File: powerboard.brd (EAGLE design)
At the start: 90 x 21 mm, 25 parts, among them IC1 ISL9122AIRNZ-T, U1 MCP73831T-2DCI/MC, U2 MIC826RYMT-TR

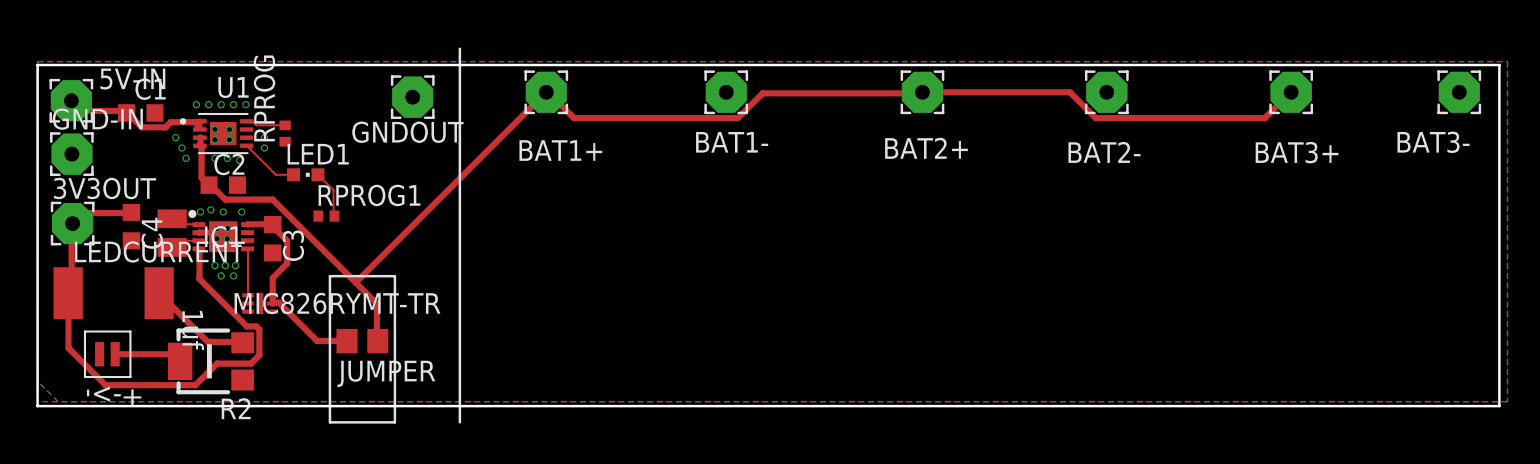
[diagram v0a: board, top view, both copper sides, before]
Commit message: update powerboard with fixes
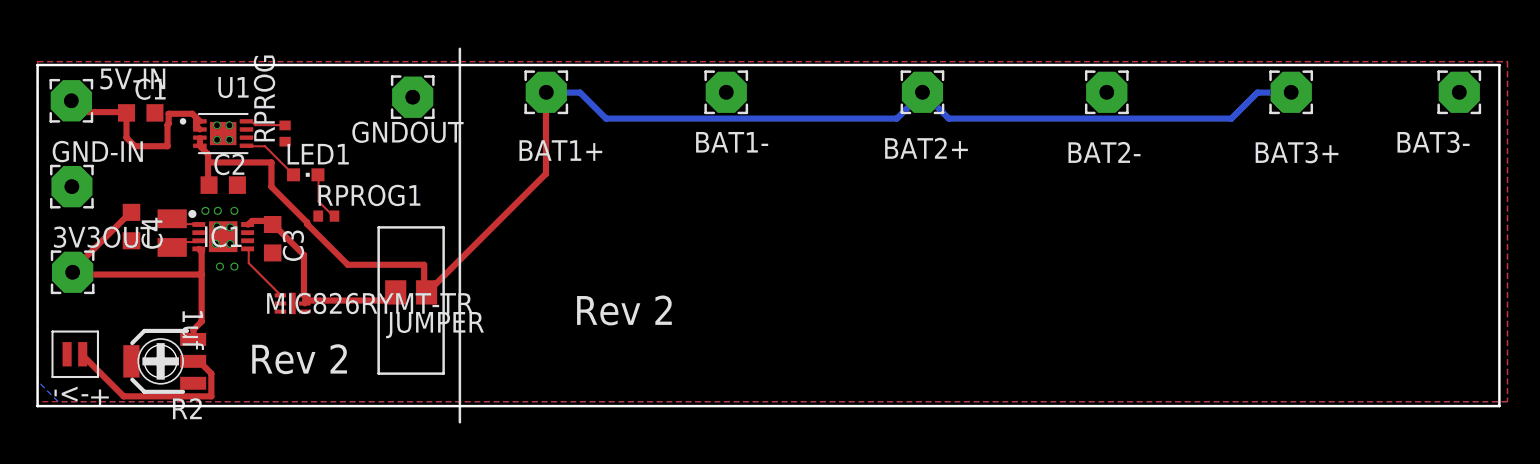
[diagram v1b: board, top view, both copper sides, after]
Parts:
- removed LEDCURRENT: 0, rcl:R2512
- R2: device rcl:RTRIMCVR42A -> rcl:RTRIM3165W
- moved JUMPER 4.24 mm to (23.0, 8.00)
- moved R2 3.00 mm to (7.58, 3.75)
- moved 3V3OUT 3.00 mm to (2.16, 9.24)
- moved GND-IN 2.00 mm to (2.11, 14.5)
- moved U2 2.00 mm to (15.7, 7.32)
- moved U$1 2.00 mm to (2.32, 4.19)
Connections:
- removed net N$2: LEDCURRENT.2, R2.3
- net 3.3REGULATED: now also R2.3; no longer LEDCURRENT.1
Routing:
- net 3.3REGULATED: track 33.6 -> 19.1 mm
- net LED+: track 4.20 -> 11.9 mm
- net N$2: track 6.41 -> 0.00 mm
- net 5VIN: track 8.77 -> 13.3 mm
- net JUMPER: track 83.9 -> 85.7 mm
- net GND: track 1.61 -> 0.00 mm, vias 0 -> 13
- net BAT_IN: track 12.8 -> 13.6 mm
- net N$10: track 2.88 -> 3.69 mm
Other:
- board text added: "Rev 2"
